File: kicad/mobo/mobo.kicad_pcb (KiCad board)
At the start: 4 copper layers, 22 x 58 mm, 9 parts, among them J1 nice!view, J12 columns, J2 Battery, J4 sensor, J8 rgb, J9 rows, SW1 Power, SW2 Reset, U1 nice!nano v2

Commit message: Cleaning up the schematics
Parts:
- removed J1: nice!view, display:OLED-128x32-double-sided
- removed J12: columns, Connector_Wuerth:Wuerth_WR-WTB_64800711622_1x07_P1.50mm_Vertical
- removed J4: sensor, Connector_Wuerth:Wuerth_WR-WTB_64800611622_1x06_P1.50mm_Vertical
- removed J9: rows, Connector_Wuerth:Wuerth_WR-WTB_64800411622_1x04_P1.50mm_Vertical
- added C1: 100n, Capacitor_SMD:C_0402_1005Metric, F.Cu at (143.2, 58.7)
- added C10: 560pF/680pF, Capacitor_SMD:C_0603_1608Metric_Pad1.08x0.95mm_HandSolder, F.Cu at (116.8, 53.4)
- added C11: 100n, Capacitor_SMD:C_0402_1005Metric, F.Cu at (146.0, 66.6)
- added C12: 1uF, Capacitor_SMD:C_0603_1608Metric_Pad1.08x0.95mm_HandSolder, F.Cu at (116.8, 55.9)
- added C13: 1uF, Capacitor_SMD:C_0603_1608Metric_Pad1.08x0.95mm_HandSolder, F.Cu at (116.8, 58.4)
- added C2: 12p, Capacitor_SMD:C_0402_1005Metric, F.Cu at (143.2, 60.6)
- added C3: 12p, Capacitor_SMD:C_0402_1005Metric, F.Cu at (143.2, 62.6)
- added C4: 1u, Capacitor_SMD:C_0402_1005Metric, F.Cu at (143.2, 64.6)
- added C5: 4u7, Capacitor_SMD:C_0402_1005Metric, F.Cu at (143.2, 66.6)
- added C6: 4u7, Capacitor_SMD:C_0402_1005Metric, F.Cu at (146.0, 58.7)
- added C7: 4u7, Capacitor_SMD:C_0402_1005Metric, F.Cu at (146.0, 60.6)
- added C8: 4u7, Capacitor_SMD:C_0402_1005Metric, F.Cu at (146.0, 62.6)
- added C9: 4u7, Capacitor_SMD:C_0402_1005Metric, F.Cu at (146.0, 64.6)
- added D1: BSD3C051V, Diode_SMD:D_SOD-323, F.Cu at (149.6, 70.4)
- added F1: 750 mA, Fuse:Fuse_0603_1608Metric, F.Cu at (116.6, 68.5)
- added FB1: Ferrite_Bead_Small, Resistor_SMD:R_0805_2012Metric_Pad1.20x1.40mm_HandSolder, F.Cu at (149.8, 59.2)
- added FB2: Ferrite_Bead_Small, Resistor_SMD:R_0805_2012Metric_Pad1.20x1.40mm_HandSolder, F.Cu at (149.8, 62.1)
- added J3: columns, Connector_Wuerth:Wuerth_WR-WTB_64800711622_1x07_P1.50mm_Vertical, F.Cu at (121.5, 54.5)
- added J5: sensor, Connector_Wuerth:Wuerth_WR-WTB_64800611622_1x06_P1.50mm_Vertical, F.Cu at (135.5, 54.5)
- added J6: rgb, Connector_Wuerth:Wuerth_WR-WTB_64800311622_1x03_P1.50mm_Vertical, F.Cu at (148.1, 54.5)
- added J7: Battery, Connector_JST:JST_ZH_S2B-ZR-SM4A-TF_1x02-1MP_P1.50mm_Horizontal, B.Cu at (198.1, 85.3)
- added L1: BLM15PX121SN1D, Inductor_SMD:L_0402_1005Metric, F.Cu at (134.4, 58.7)
- added L2: BLM15PX121SN1D, Inductor_SMD:L_0402_1005Metric, F.Cu at (134.4, 60.7)
- added L3: 10 uH, Inductor_SMD:L_0603_1608Metric, F.Cu at (116.6, 71.0)
- added LED1: orange, LED_SMD:LED_0402_1005Metric, F.Cu at (130.7, 67.7)
- added Q1: 2N7002, Package_TO_SOT_SMD:SOT-23, F.Cu at (121.4, 60.1)
- added Q2: AO3401A, Package_TO_SOT_SMD:SOT-23, F.Cu at (121.4, 64.7)
- added Q3: 2N7002, Package_TO_SOT_SMD:SOT-23, F.Cu at (121.4, 69.3)
- added R1: 5k1, Resistor_SMD:R_0402_1005Metric, F.Cu at (134.4, 62.7)
- added R10: 1k5, Resistor_SMD:R_0402_1005Metric, F.Cu at (137.4, 68.6)
- added R11: 100R, Resistor_SMD:R_0402_1005Metric, F.Cu at (140.3, 58.7)
- added R12: 10k, Resistor_SMD:R_0402_1005Metric, F.Cu at (140.3, 60.7)
- added R13: 100k, Resistor_SMD:R_0402_1005Metric, F.Cu at (140.3, 62.7)
- added R14: 10k, Resistor_SMD:R_0603_1608Metric_Pad0.98x0.95mm_HandSolder, F.Cu at (116.8, 60.9)
- added R15: 10k, Resistor_SMD:R_0603_1608Metric_Pad0.98x0.95mm_HandSolder, F.Cu at (116.8, 63.4)
- added R16: 10k, Resistor_SMD:R_0603_1608Metric_Pad0.98x0.95mm_HandSolder, F.Cu at (116.8, 66.0)
- added R17: 5k1, Resistor_SMD:R_0402_1005Metric, F.Cu at (140.3, 64.7)
- added R18: 5k1, Resistor_SMD:R_0402_1005Metric, F.Cu at (140.3, 66.7)
- added R2: 5k1, Resistor_SMD:R_0402_1005Metric, F.Cu at (134.4, 64.7)
- added R3: 100R, Resistor_SMD:R_0402_1005Metric, F.Cu at (134.4, 66.7)
- added R4: 10k, Resistor_SMD:R_0402_1005Metric, F.Cu at (134.4, 68.6)
- added R5: 47k, Resistor_SMD:R_0402_1005Metric, F.Cu at (137.4, 58.7)
- added R6: 10k, Resistor_SMD:R_0402_1005Metric, F.Cu at (137.4, 60.7)
- added R7: 1k5, Resistor_SMD:R_0402_1005Metric, F.Cu at (137.4, 62.7)
- added R8: 3k9, Resistor_SMD:R_0402_1005Metric, F.Cu at (137.4, 64.7)
- added R9: 10k, Resistor_SMD:R_0402_1005Metric, F.Cu at (137.4, 66.7)
- added U2: SRV05-4, Package_TO_SOT_SMD:SOT-23-6, F.Cu at (126.4, 69.1)
- added U3: BQ24075, Package_DFN_QFN:VQFN-16-1EP_3x3mm_P0.5mm_EP1.6x1.6mm, F.Cu at (150.1, 66.2)
- added Y1: 32.768 KHz, Crystal:Crystal_SMD_2012-2Pin_2.0x1.2mm, F.Cu at (143.7, 69.2)
- J2: value Battery -> HRO_TYPE-C-31-M-14; footprint Connector_JST:JST_ZH_S2B-ZR-SM4A-TF_1x02-1MP_P1.50mm_Horizontal -> Connector_USB:USB_C_Receptacle_HRO_TYPE-C-31-M-12
- J8: value rgb -> Conn_01x10; footprint Connector_Wuerth:Wuerth_WR-WTB_64800311622_1x03_P1.50mm_Vertical -> Connector_FFC-FPC:Hirose_FH12-10S-0.5SH_1x10-1MP_P0.50mm_Horizontal
- SW1: value Power -> Reset; footprint Button_Switch_SMD:SW_SPDT_PCM12 -> Button_Switch_SMD:SW_SPST_B3U-1000P
- SW2: value Reset -> PWR
- U1: value nice!nano v2 -> nRF52840_E73-2G4M08S1C; footprint keyboard_reversible:ProMicro_independent_flipped -> E73-2G4M08S1C Model:E73-2G4M08S1C; moved to B.Cu
- moved J2 51.6 mm to (193.4, 34.1), turned to 180 degrees
- moved J8 31.2 mm to (193.6, 68.2), turned to 0 degrees
- moved U1 3.19 mm to (193.2, 51.6), turned to 0 degrees
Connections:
- J8 pad 1: RGB -> LCD_CLK
- J8 pad 2: GND -> LCD_IN
- J8 pad 3: VCC -> LCD_CS
- SW1 pad 1: Net-(J2-Pin_2) -> VSS
- SW1 pad 2: BAT -> RST
- SW2 pad 1: GND -> Net-(SW2-A)
- SW2 pad 2: RST -> SYSOFF
- U1 pad 1: RGB -> unconnected-(U1-P1.11-Pad1)
- U1 pad 10: Row 1 -> row1
- U1 pad 11: Row 2 -> Net-(U1-P0.00/XL1)
- U1 pad 12: Row 3 -> unconnected-(U1-P0.26-Pad12)
- U1 pad 13: unconnected-(U1-10-Pad13) -> Net-(U1-P0.01/XL2)
- U1 pad 14: Col 6 -> unconnected-(U1-P0.06-Pad14)
- U1 pad 15: Col 5 -> SCL
- U1 pad 16: Col 4 -> unconnected-(U1-P0.08-Pad16)
- U1 pad 17: Col 3 -> unconnected-(U1-P1.09-Pad17)
- U1 pad 18: Col 2 -> unconnected-(U1-P0.04/AIN2-Pad18)
- U1 pad 19: Col 1 -> VDD
- U1 pad 2: SCK -> unconnected-(U1-P1.10-Pad2)
- U1 pad 20: Col 0 -> unconnected-(U1-P0.12-Pad20)
- U1 pad 21: VCC -> VSS
- U1 pad 22: RST -> SDA
- U1 pad 23: GND -> +VSW
- U1 pad 24: BAT -> VSS
- U1 pad 3: GND -> unconnected-(U1-P0.03/AIN1-Pad3)
- U1 pad 4: GND -> col1
- U1 pad 5: SDIO -> VSS
- U1 pad 6: IRQ -> unconnected-(U1-P1.13-Pad6)
- U1 pad 7: CS_D -> col0
- U1 pad 8: CS_T -> row0
- U1 pad 9: Row 0 -> unconnected-(U1-P0.31/AIN7-Pad9)
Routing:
- net GND: track 185.4 -> 0.00 mm, vias 3 -> 0
- net VCC: track 117.2 -> 0.00 mm, vias 1 -> 0
- net SCK: track 116.6 -> 0.00 mm, vias 1 -> 0
- net SDIO: track 94.3 -> 0.00 mm, vias 1 -> 0
- net BAT: track 65.7 -> 0.00 mm, vias 2 -> 0
- net CS_D: track 50.6 -> 0.00 mm, vias 1 -> 0
- net RST: track 49.7 -> 0.00 mm, vias 2 -> 0
- net IRQ: track 45.6 -> 0.00 mm, vias 1 -> 0
- net CS_T: track 35.9 -> 0.00 mm, vias 1 -> 0
- net Net-(J2-Pin_2): track 29.1 -> 0.00 mm
- net Col 6: track 27.7 -> 0.00 mm, vias 1 -> 0
- net Col 5: track 27.1 -> 0.00 mm, vias 1 -> 0
- net Col 0: track 26.3 -> 0.00 mm, vias 1 -> 0
- net Col 4: track 26.2 -> 0.00 mm, vias 1 -> 0
- net Col 1: track 25.9 -> 0.00 mm, vias 1 -> 0
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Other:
- board text removed: "1"
- board text removed: "24"
- board text removed: "columns"
- board text removed: "nice!nano"
- board text removed: "nice!view"
- board text removed: "rgb"
- board text removed: "rows"
- board text removed: "sensor"

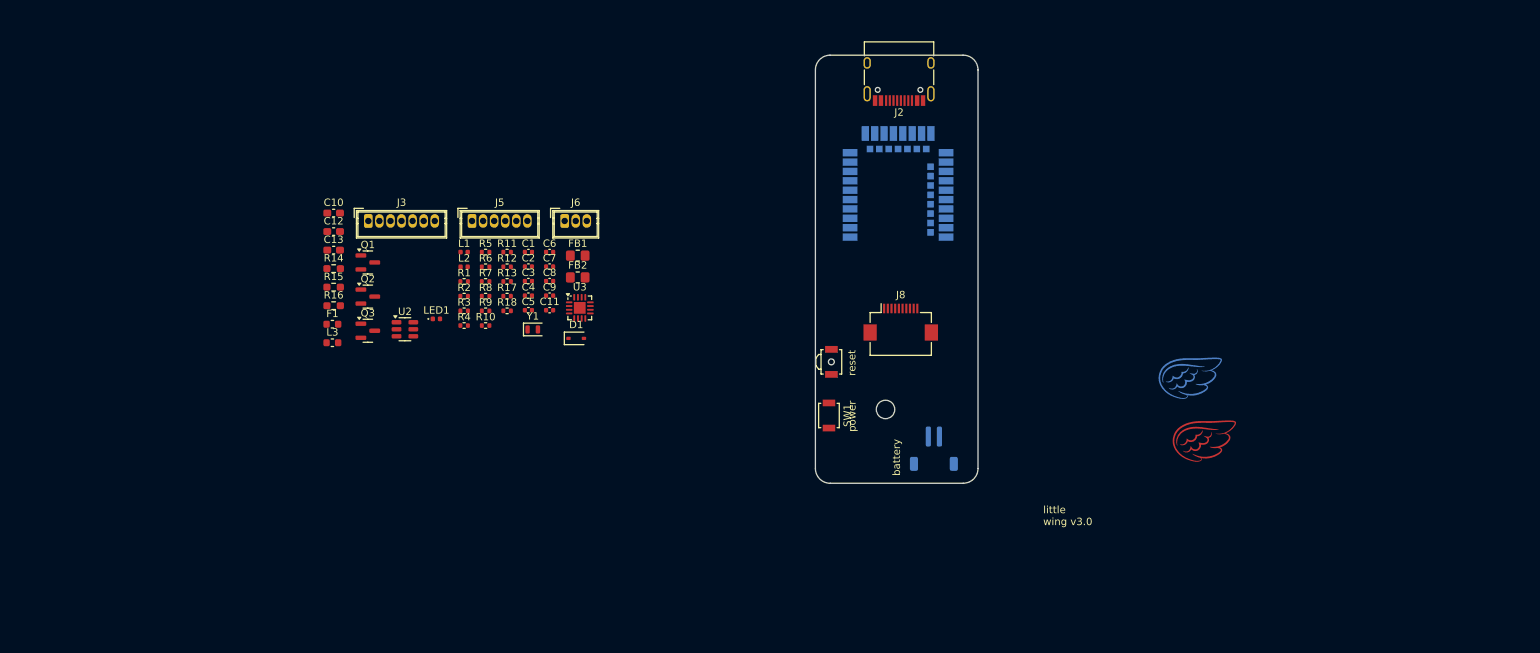
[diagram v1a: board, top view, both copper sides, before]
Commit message: Resetting the PCB
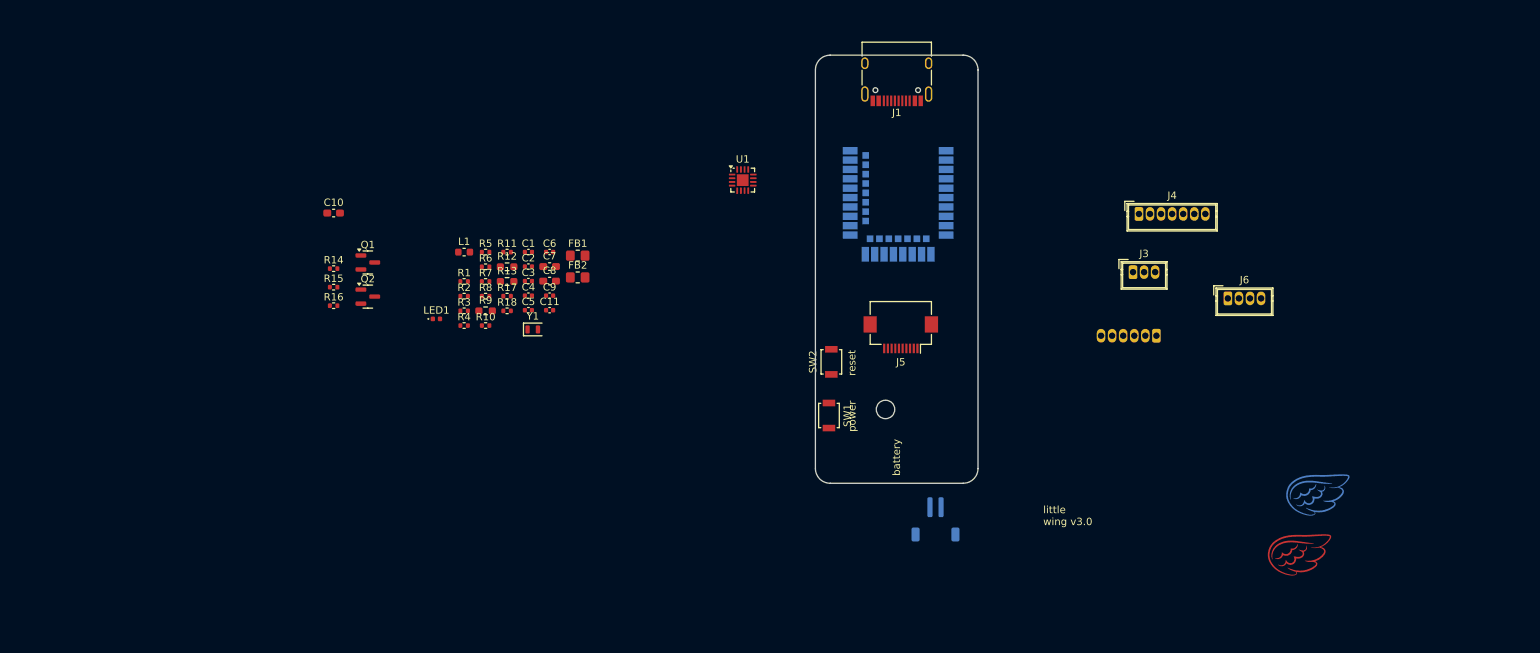
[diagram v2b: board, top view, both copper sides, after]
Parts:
- removed C12, C13: 1uF, Capacitor_SMD:C_0603_1608Metric_Pad1.08x0.95mm_HandSolder
- removed D1: BSD3C051V, Diode_SMD:D_SOD-323
- removed F1: 750 mA, Fuse:Fuse_0603_1608Metric
- removed J8: Conn_01x10, Connector_FFC-FPC:Hirose_FH12-10S-0.5SH_1x10-1MP_P0.50mm_Horizontal
- removed L2: BLM15PX121SN1D, Inductor_SMD:L_0402_1005Metric
- removed L3: 10 uH, Inductor_SMD:L_0603_1608Metric
- removed Q3: 2N7002, Package_TO_SOT_SMD:SOT-23
- removed U3: BQ24075, Package_DFN_QFN:VQFN-16-1EP_3x3mm_P0.5mm_EP1.6x1.6mm
- added J1: HRO_TYPE-C-31-M-14, Connector_USB:USB_C_Receptacle_HRO_TYPE-C-31-M-12, F.Cu at (193.1, 34.1)
- added J4: columns, Connector_Wuerth:Wuerth_WR-WTB_64800711622_1x07_P1.50mm_Vertical, F.Cu at (225.9, 53.5)
- C1: value 100n -> 4u7
- C10: value 560pF/680pF -> 1uF
- C11: value 100n -> 12p
- C2, C3: value 12p -> 4u7
- C7: value 4u7 -> 560pF/680pF; footprint Capacitor_SMD:C_0402_1005Metric -> Capacitor_SMD:C_0603_1608Metric_Pad1.08x0.95mm_HandSolder
- C8: value 4u7 -> 1uF; footprint Capacitor_SMD:C_0402_1005Metric -> Capacitor_SMD:C_0603_1608Metric_Pad1.08x0.95mm_HandSolder
- C9: value 4u7 -> 12p
- J2: value HRO_TYPE-C-31-M-14 -> Battery; footprint Connector_USB:USB_C_Receptacle_HRO_TYPE-C-31-M-12 -> Connector_JST:JST_ZH_S2B-ZR-SM4A-TF_1x02-1MP_P1.50mm_Horizontal; moved to B.Cu
- J3: value columns -> rgb; footprint Connector_Wuerth:Wuerth_WR-WTB_64800711622_1x07_P1.50mm_Vertical -> Connector_Wuerth:Wuerth_WR-WTB_64800311622_1x03_P1.50mm_Vertical
- J5: value sensor -> Conn_01x10; footprint Connector_Wuerth:Wuerth_WR-WTB_64800611622_1x06_P1.50mm_Vertical -> Connector_FFC-FPC:Hirose_FH12-10S-0.5SH_1x10-1MP_P0.50mm_Horizontal
- J6: value rgb -> rows; footprint Connector_Wuerth:Wuerth_WR-WTB_64800311622_1x03_P1.50mm_Vertical -> Connector_Wuerth:Wuerth_WR-WTB_64800411622_1x04_P1.50mm_Vertical
- J7: value Battery -> sensor; footprint Connector_JST:JST_ZH_S2B-ZR-SM4A-TF_1x02-1MP_P1.50mm_Horizontal -> Connector_Wuerth:Wuerth_WR-WTB_64800611622_1x06_P1.50mm_Vertical
- L1: value BLM15PX121SN1D -> 10 uH; footprint Inductor_SMD:L_0402_1005Metric -> Inductor_SMD:L_0603_1608Metric
- Q1: value 2N7002 -> AO3401A
- Q2: value AO3401A -> 2N7002
- R10: value 1k5 -> 10k
- R12, R9: footprint Resistor_SMD:R_0402_1005Metric -> Resistor_SMD:R_0603_1608Metric_Pad0.98x0.95mm_HandSolder
- R13: value 100k -> 10k; footprint Resistor_SMD:R_0402_1005Metric -> Resistor_SMD:R_0603_1608Metric_Pad0.98x0.95mm_HandSolder
- R14, R15, R16: value 10k -> 100R; footprint Resistor_SMD:R_0603_1608Metric_Pad0.98x0.95mm_HandSolder -> Resistor_SMD:R_0402_1005Metric
- R17: value 5k1 -> 100R
- R18: value 5k1 -> 10k
- R3: value 100R -> 10k
- R4, R6: value 10k -> 1k5
- R7: value 1k5 -> 3k9
- R8: value 3k9 -> 100R
- SW1: value Reset -> Battery
- SW2: value PWR -> Reset; footprint Button_Switch_SMD:SW_SPST_B3U-3000P-B -> Button_Switch_SMD:SW_SPST_B3U-1000P
- U1: value nRF52840_E73-2G4M08S1C -> BQ24075; footprint E73-2G4M08S1C Model:E73-2G4M08S1C -> Package_DFN_QFN:VQFN-16-1EP_3x3mm_P0.5mm_EP1.6x1.6mm; moved to F.Cu
- U2: value SRV05-4 -> nRF52840_E73-2G4M08S1C; footprint Package_TO_SOT_SMD:SOT-23-6 -> E73-2G4M08S1C Model:E73-2G4M08S1C; moved to B.Cu
- moved J3 103.8 mm to (225.1, 61.4)
- moved J6 90.5 mm to (237.9, 65.0)
- moved U2 69.5 mm to (193.2, 50.0), turned to 180 degrees
- moved J2 61.0 mm to (198.3, 94.9)
- moved J5 60.1 mm to (193.6, 69.9), turned to 180 degrees
- moved J7 33.8 mm to (228.2, 70.0)
- moved U1 21.2 mm to (172.2, 48.9)
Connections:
- net RGB renamed Row 0
- C1 pad 1: Earth -> +5V
- C1 pad 2: VSS -> GND
- C10 pad 1: DISP -> VDDA
- C10 pad 2: VSS -> GNDA
- C11 pad 1: VSS -> Net-(U2-P0.01/XL2)
- C11 pad 2: +BATT -> GND
- C2 pad 1: Net-(U1-P0.00/XL1) -> +VSW
- C2 pad 2: VSS -> GND
- C3 pad 1: Net-(U1-P0.01/XL2) -> +BATT
- C3 pad 2: VSS -> GND
- C4 pad 2: VSS -> GND
- C5 pad 2: VSS -> GND
- C6 pad 1: +5V -> +VSW
- C6 pad 2: VSS -> GND
- C7 pad 1: +VSW -> Net-(J5-Pin_5)
- C7 pad 2: VSS -> GND
- C8 pad 1: +BATT -> VDD
- C8 pad 2: VSS -> GND
- C9 pad 1: +VSW -> Net-(U2-P0.00/XL1)
- C9 pad 2: VSS -> GND
- FB2 pad 1: VSS -> GND
- FB2 pad 2: VSSA -> GNDA
- J3 pad 1: Col 0 -> RGB_PWR
- J3 pad 2: Col 1 -> Net-(J3-Pin_2)
- J3 pad 3: Col 2 -> GND
- J5 pad 1: VDD -> LCD_CLK
- J5 pad 2: SESOR_CS -> LCD_IN
- J5 pad 3: SENSOR_SDIO -> LCD_CS
- J5 pad 4: SENSOR_SCK -> EXTCOMIN
- J5 pad 5: SENSOR_IRQ -> Net-(J5-Pin_5)
- J5 pad 6: VSS -> VDDA
- J6 pad 2: VSS -> Row 1
- J6 pad 3: UG_PWR -> Row 2
- J7 pad 1: VSS -> VDD
- J7 pad 2: +BATT -> Net-(J7-Pin_2)
- L1 pad 1: Earth -> DCCH
- L1 pad 2: VSS -> VDD
- Q1 pad 2: VSS -> +VSW
- Q1 pad 3: Net-(Q1-D) -> RGB_PWR
- Q2 pad 1: Net-(Q1-D) -> Net-(Q2-G)
- Q2 pad 2: +VSW -> GND
- Q2 pad 3: UG_PWR -> Net-(Q1-G)
- R1 pad 1: GNDPWR -> GND
- R1 pad 2: Net-(J2-CC2) -> Net-(J1-CC1)
- R10 pad 1: Net-(LED1-K) -> +VSW
- R10 pad 2: Net-(U3-~{CHG}) -> Net-(Q1-G)
- R11 pad 1: +5V -> SESOR_CS
- R11 pad 2: Net-(Q3-G) -> Net-(J7-Pin_2)
- R12 pad 1: Net-(Q3-G) -> EXTMODE
- R12 pad 2: VSS -> GND
- R13 pad 1: Net-(SW2-A) -> EXTCOMIN
- R13 pad 2: +BATT -> GND
- R14 pad 1: VDD -> SENSOR_SDIO
- R14 pad 2: DISP -> Net-(J7-Pin_3)
- R15 pad 1: EXTMODE -> SENSOR_SCK
- R15 pad 2: VSS -> Net-(J7-Pin_4)
- R16 pad 1: EXTCOMIN -> SENSOR_IRQ
- R16 pad 2: VSS -> Net-(J7-Pin_5)
- R17 pad 1: SDA -> RGB_ON
- R17 pad 2: VDD -> Net-(Q2-G)
- R18 pad 1: SCL -> Net-(Q2-G)
- R18 pad 2: VDD -> GND
- R2 pad 1: GNDPWR -> GND
- R2 pad 2: Net-(J2-CC1) -> Net-(J1-CC2)
- R3 pad 1: UG_EN -> Net-(U1-TS)
- R3 pad 2: Net-(Q1-G) -> GND
- R4 pad 1: Net-(Q1-G) -> Net-(LED1-K)
- R4 pad 2: VSS -> Net-(U1-~{CHG})
- R5 pad 2: VSS -> GND
- R6 pad 1: +VSW -> /ILIM
- R6 pad 2: Net-(Q1-D) -> GND
- R7 pad 1: /ILIM -> Net-(U1-ISET)
- R7 pad 2: VSS -> GND
- R8 pad 1: Net-(U3-ISET) -> RGB_DATA
- R8 pad 2: VSS -> Net-(J3-Pin_2)
- R9 pad 1: Net-(U3-TS) -> VDD
- R9 pad 2: VSS -> Net-(J5-Pin_5)
- SW1 pad 1: VSS -> Net-(J2-Pin_1)
- SW1 pad 2: RST -> +BATT
- SW2 pad 1: Net-(SW2-A) -> GND
- SW2 pad 2: SYSOFF -> RST
- U1 pad 1: unconnected-(U1-P1.11-Pad1) -> Net-(U1-TS)
- U1 pad 10: row1 -> +VSW
- U1 pad 11: Net-(U1-P0.00/XL1) -> +VSW
- U1 pad 12: unconnected-(U1-P0.26-Pad12) -> /ILIM
- U1 pad 13: Net-(U1-P0.01/XL2) -> +5V
- U1 pad 14: unconnected-(U1-P0.06-Pad14) -> /TMR
- U1 pad 15: SCL -> unconnected-(U1-SYSOFF-Pad15)
- U1 pad 16: unconnected-(U1-P0.08-Pad16) -> Net-(U1-ISET)
- U1 pad 17: unconnected-(U1-P1.09-Pad17) -> GND
- U1 pad 2: unconnected-(U1-P1.10-Pad2) -> +BATT
- U1 pad 3: unconnected-(U1-P0.03/AIN1-Pad3) -> +BATT
- U1 pad 4: col1 -> GND
- U1 pad 5: VSS -> GND
- U1 pad 6: unconnected-(U1-P1.13-Pad6) -> +VSW
- U1 pad 7: col0 -> unconnected-(U1-~{PGOOD}-Pad7)
- U1 pad 8: row0 -> GND
- U1 pad 9: unconnected-(U1-P0.31/AIN7-Pad9) -> Net-(U1-~{CHG})
- U2 pad 1: USB-D- -> unconnected-(U2-P1.11-Pad1)
- U2 pad 2: VSS -> unconnected-(U2-P1.10-Pad2)
- U2 pad 5: +5V -> GND
- U2 pad 6: USB-D+ -> unconnected-(U2-P1.13-Pad6)
- Y1 pad 1: Net-(U1-P0.01/XL2) -> Net-(U2-P0.01/XL2)
- Y1 pad 2: Net-(U1-P0.00/XL1) -> Net-(U2-P0.00/XL1)

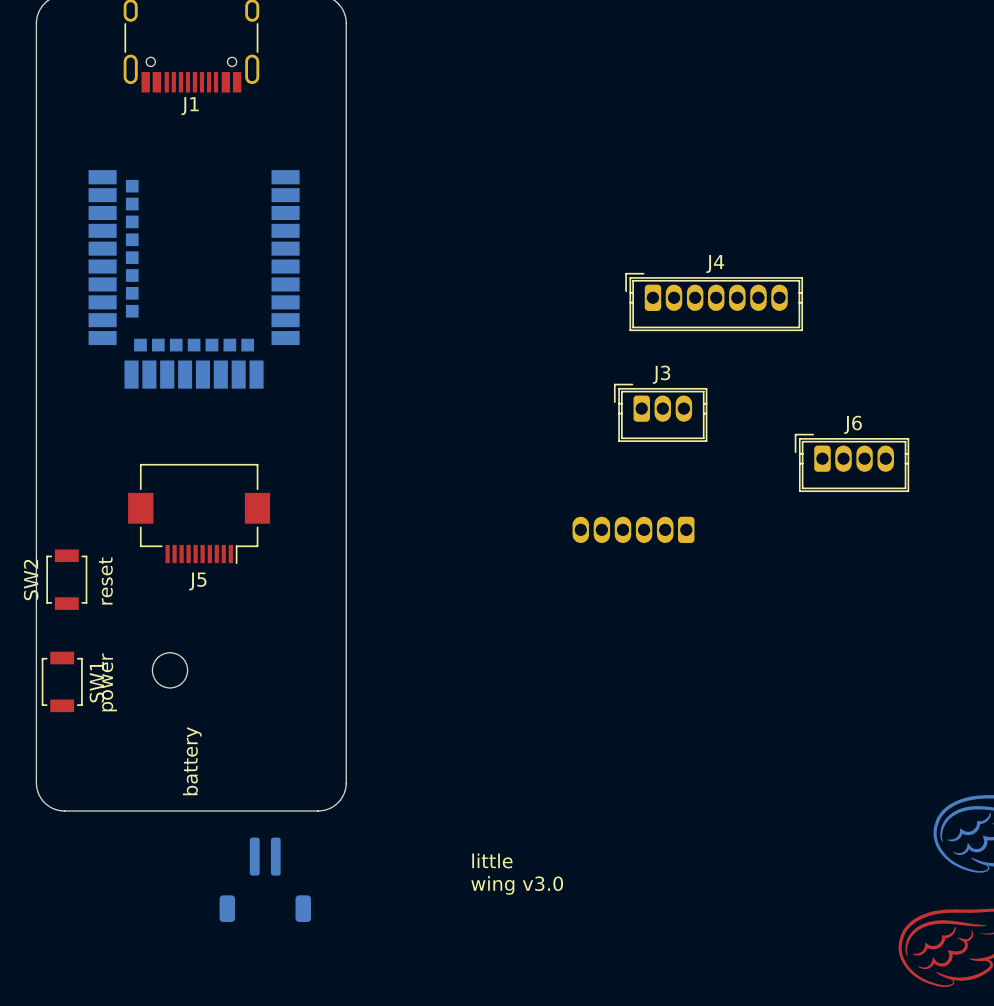
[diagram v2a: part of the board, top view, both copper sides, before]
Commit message: Replacing the through holes with JST-SH connectors
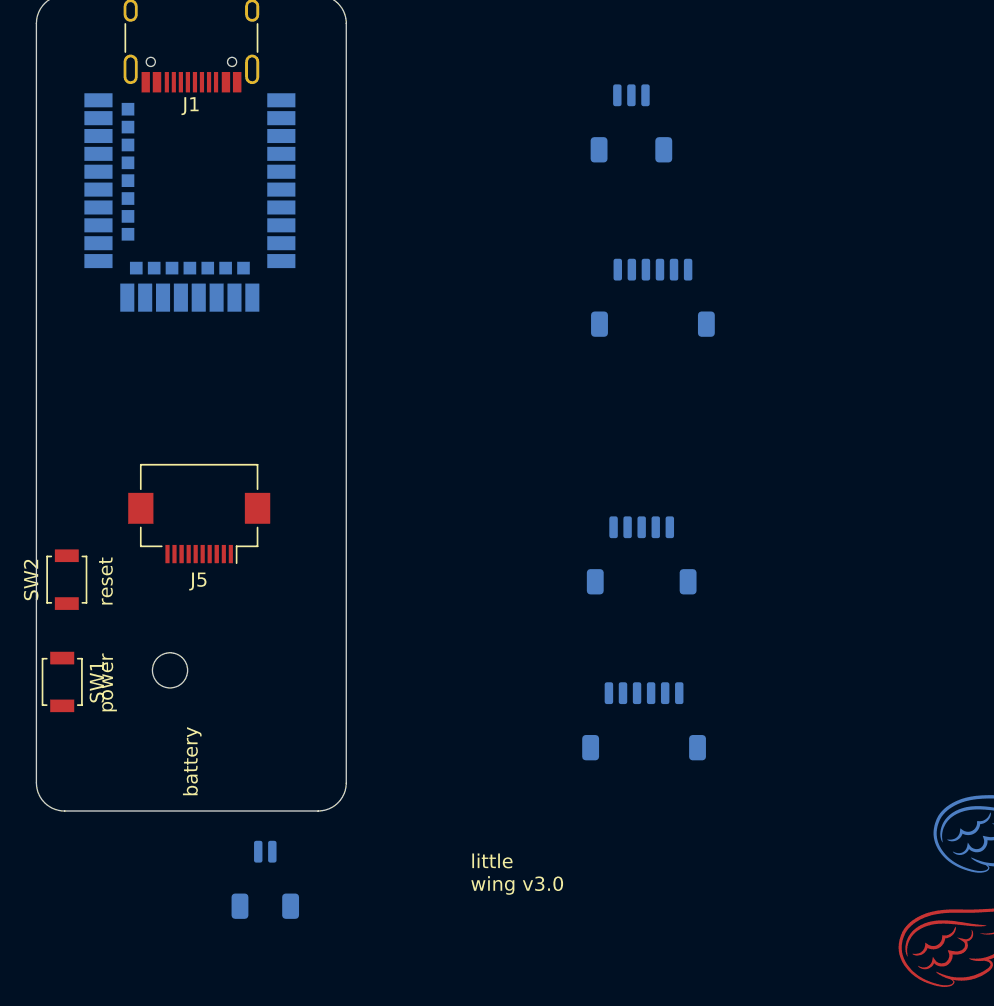
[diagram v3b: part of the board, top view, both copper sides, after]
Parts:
- J2: footprint Connector_JST:JST_ZH_S2B-ZR-SM4A-TF_1x02-1MP_P1.50mm_Horizontal -> Connector_JST:JST_SH_SM02B-SRSS-TB_1x02-1MP_P1.00mm_Horizontal
- J3: footprint Connector_Wuerth:Wuerth_WR-WTB_64800311622_1x03_P1.50mm_Vertical -> Connector_JST:JST_SH_SM03B-SRSS-TB_1x03-1MP_P1.00mm_Horizontal; moved to B.Cu
- J4: footprint Connector_Wuerth:Wuerth_WR-WTB_64800711622_1x07_P1.50mm_Vertical -> Connector_JST:JST_SH_SM06B-SRSS-TB_1x06-1MP_P1.00mm_Horizontal; moved to B.Cu
- J6: footprint Connector_Wuerth:Wuerth_WR-WTB_64800411622_1x04_P1.50mm_Vertical -> Connector_JST:JST_SH_SM05B-SRSS-TB_1x05-1MP_P1.00mm_Horizontal; moved to B.Cu
- J7: footprint Connector_Wuerth:Wuerth_WR-WTB_64800611622_1x06_P1.50mm_Vertical -> Connector_JST:JST_SH_SM06B-SRSS-TB_1x06-1MP_P1.00mm_Horizontal
- moved J3 20.3 mm to (224.3, 41.1), turned to 180 degrees
- moved J6 14.6 mm to (225.1, 71.8), turned to 180 degrees
- moved J7 13.9 mm to (225.2, 83.6)
- moved U2 5.48 mm to (192.9, 44.5)
- turned J4 to 180 degrees
